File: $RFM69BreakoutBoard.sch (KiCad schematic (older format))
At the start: 22 parts, among them P1 BB Holes, P10 TST, P11 ANA hole, P2 TST, P3 TST, P4 TST, P5 TST, P6 TST, P7 TST, P8 TST, P9 TST, U1 MCP1703, U2 74LVC245, U3 RFM69HW

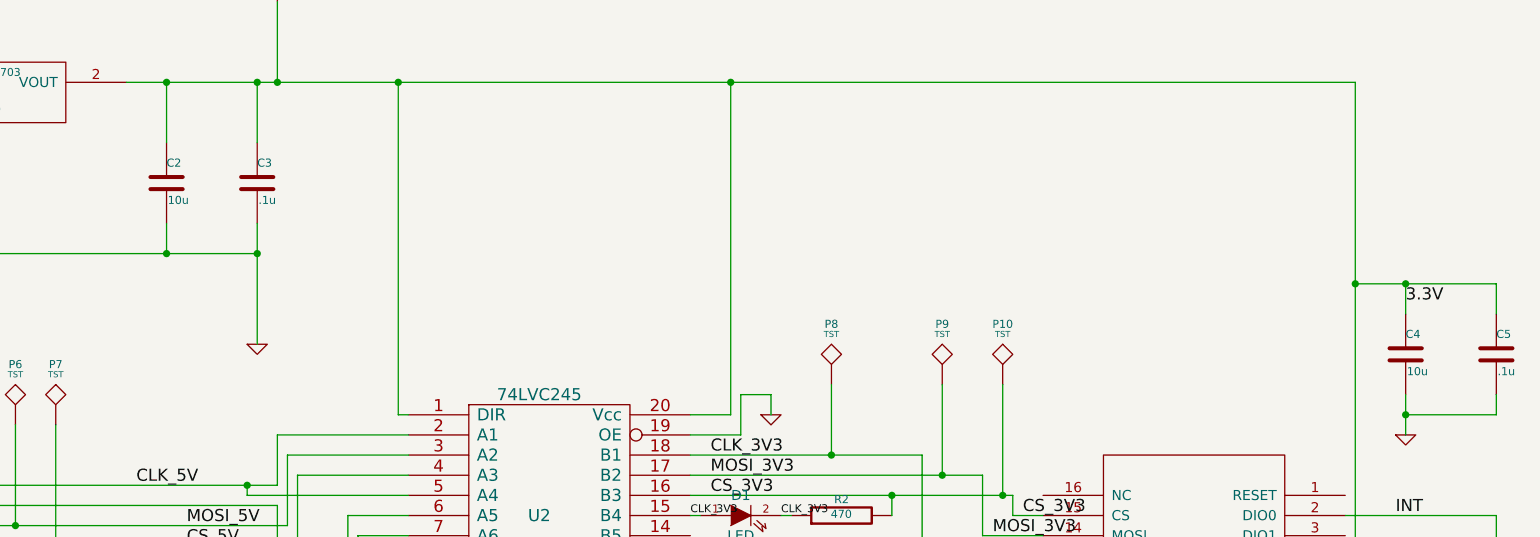
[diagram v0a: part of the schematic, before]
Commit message: update to test points.  Changed electrolytic 10uF caps to ceramic
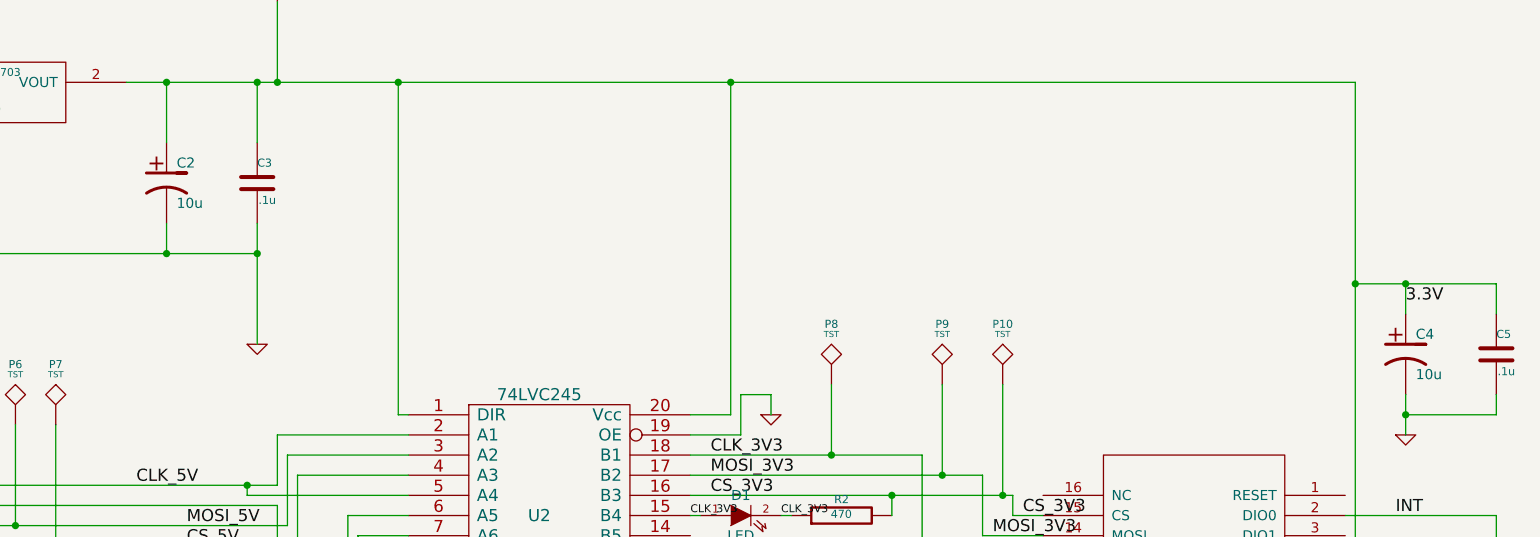
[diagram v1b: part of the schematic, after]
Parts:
- removed C2, C4: 10u, ~, symbol C
- added C2, C4: 10u, ~, symbol CP1
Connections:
- net +3.3V: now also C2.1, C4.1
- net GND: now also C2.2, C4.2
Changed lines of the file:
@@
 $EndComp
 $Comp
-L GND #PWR5
+L GND #PWR01
 U 1 1 5305B481
 P 4400 3600
-F 0 "#PWR5" H 4400 3600 30  0001 C CNN
+F 0 "#PWR01" H 4400 3600 30  0001 C CNN
 F 1 "GND" H 4400 3530 30  0001 C CNN
 F 2 "" H 4400 3600 60  0000 C CNN
@@
 5V
 $Comp
-L +5V #PWR2
+L +5V #PWR02
 U 1 1 5307CDEB
 P 1950 1900
-F 0 "#PWR2" H 1950 1990 20  0001 C CNN
+F 0 "#PWR02" H 1950 1990 20  0001 C CNN
 F 1 "+5V" H 1950 1990 30  0000 C CNN
 F 2 "" H 1950 1900 60  0000 C CNN
@@
 CS_3V3
 $Comp
-L GND #PWR7
+L GND #PWR03
 U 1 1 530BB7C1
 P 4800 4950
-F 0 "#PWR7" H 4800 4950 30  0001 C CNN
+F 0 "#PWR03" H 4800 4950 30  0001 C CNN
 F 1 "GND" H 4800 4880 30  0001 C CNN
 F 2 "" H 4800 4950 60  0000 C CNN
@@
 CLK_5V
 $Comp
-L GND #PWR8
+L GND #PWR04
 U 1 1 530BC03D
 P 6950 3950
-F 0 "#PWR8" H 6950 3950 30  0001 C CNN
+F 0 "#PWR04" H 6950 3950 30  0001 C CNN
 F 1 "GND" H 6950 3880 30  0001 C CNN
 F 2 "" H 6950 3950 60  0000 C CNN
@@
 $EndComp
 $Comp
-L GND #PWR1
+L GND #PWR05
 U 1 1 530CAAF5
 P 1800 6350
-F 0 "#PWR1" H 1800 6350 30  0001 C CNN
+F 0 "#PWR05" H 1800 6350 30  0001 C CNN
 F 1 "GND" H 1800 6280 30  0001 C CNN
 F 2 "" H 1800 6350 60  0000 C CNN
@@
 $EndComp
 $Comp
-L GND #PWR9
+L GND #PWR06
 U 1 1 530DFEA1
 P 10100 4050
-F 0 "#PWR9" H 10100 4050 30  0001 C CNN
+F 0 "#PWR06" H 10100 4050 30  0001 C CNN
 F 1 "GND" H 10100 3980 30  0001 C CNN
 F 2 "" H 10100 4050 60  0000 C CNN
@@
 $EndComp
 $Comp
-L +5V #PWR4
+L CP1 C4
+U 1 1 530F2E03
+P 10100 3650
+F 0 "C4" H 10150 3750 50  0000 L CNN
+F 1 "10u" H 10150 3550 50  0000 L CNN
+F 2 "~" H 10100 3650 60  0000 C CNN
+F 3 "~" H 10100 3650 60  0000 C CNN
+	1    10100 3650
+	1    0    0    -1
+$EndComp
+$Comp
+L CP1 C2
+U 1 1 530F2E4A
+P 3950 2800
+F 0 "C2" H 4000 2900 50  0000 L CNN
+F 1 "10u" H 4000 2700 50  0000 L CNN
+F 2 "~" H 3950 2800 60  0000 C CNN
+F 3 "~" H 3950 2800 60  0000 C CNN
+	1    3950 2800
+	1    0    0    -1
+$EndComp
+$Comp
+L +5V #PWR07
 U 1 1 531314FA
 P 2800 5650
-F 0 "#PWR4" H 2800 5740 20  0001 C CNN
+F 0 "#PWR07" H 2800 5740 20  0001 C CNN
 F 1 "+5V" H 2800 5740 30  0000 C CNN
 F 2 "" H 2800 5650 60  0000 C CNN
@@
 $EndComp
 $Comp
-L +5V #PWR3
+L +5V #PWR08
 U 1 1 531316EA
 P 1950 3800
-F 0 "#PWR3" H 1950 3890 20  0001 C CNN
+F 0 "#PWR08" H 1950 3890 20  0001 C CNN
 F 1 "+5V" H 1950 3890 30  0000 C CNN
 F 2 "" H 1950 3800 60  0000 C CNN
@@
 $EndComp
 $Comp
-L +3.3V #PWR6
+L +3.3V #PWR09
 U 1 1 5313177E
 P 4500 1900
-F 0 "#PWR6" H 4500 1860 30  0001 C CNN
+F 0 "#PWR09" H 4500 1860 30  0001 C CNN
 F 1 "+3.3V" H 4500 2010 30  0000 C CNN
 F 2 "" H 4500 1900 60  0000 C CNN
@@
 Wire Wire Line
 	9850 5050 9800 5050
-$Comp
-L C C2
-U 1 1 531506ED
-P 3950 2800
-F 0 "C2" H 3950 2900 40  0000 L CNN
-F 1 "10u" H 3956 2715 40  0000 L CNN
-F 2 "~" H 3988 2650 30  0000 C CNN
-F 3 "~" H 3950 2800 60  0000 C CNN
-F 4 "Yageo" H 3950 2800 60  0001 C CNN "MFG Name"
-F 5 "CC0603KRX7R7BB104" H 3950 2800 60  0001 C CNN "MFG Part Number"
-F 6 "311-1088-1-ND" H 3950 2800 60  0001 C CNN "Distributor Part Number"
-F 7 " http://www.digikey.com/product-detail/en/CC0603KRX7R7BB104/311-1088-1-ND/302998?cur=USD" H 3950 2800 60  0001 C CNN "Distributor Part Number Link"
-	1    3950 2800
-	1    0    0    -1
-$EndComp
-$Comp
-L C C4
-U 1 1 5315070F
-P 10100 3650
-F 0 "C4" H 10100 3750 40  0000 L CNN
-F 1 "10u" H 10106 3565 40  0000 L CNN
-F 2 "~" H 10138 3500 30  0000 C CNN
-F 3 "~" H 10100 3650 60  0000 C CNN
-F 4 "Yageo" H 10100 3650 60  0001 C CNN "MFG Name"
-F 5 "CC0603KRX7R7BB104" H 10100 3650 60  0001 C CNN "MFG Part Number"
-F 6 "311-1088-1-ND" H 10100 3650 60  0001 C CNN "Distributor Part Number"
-F 7 " http://www.digikey.com/product-detail/en/CC0603KRX7R7BB104/311-1088-1-ND/302998?cur=USD" H 10100 3650 60  0001 C CNN "Distributor Part Number Link"
-	1    10100 3650
-	1    0    0    -1
-$EndComp
 $EndSCHEMATC
